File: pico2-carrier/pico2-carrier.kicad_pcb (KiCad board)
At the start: 2 copper layers, 81.8 x 80.8 mm, 52 parts, among them IC1 TFBS4711-TT1, IC2 M95512-DRMN8TP_K, IC3 IS25WP128F-JBLE, IC4 BQ25628ERYKR, J2 SCREEN_HDR, J3 DO0180FMST08, J5 Ext_Pwr_Rail, SW1 BUT_L, SW2 BUT_M, SW3 BUT_R, SW4 RUN, U1 Pico 2

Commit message: start work on PCB
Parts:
- removed BZ1: Speaker, Jumper:SolderJumper-2_P1.3mm_Open_Pad1.0x1.5mm
- removed the R4 at (173.5, 135.4)
- removed the R5 at (174.5, 134.4)
- added R3: 1k, Resistor_SMD:R_0402_1005Metric, F.Cu at (109.7, 130.3)
- BT1: footprint Jumper:SolderJumper-2_P1.3mm_Open_Pad1.0x1.5mm -> Connector_JST:JST_PH_B2B-PH-K_1x02_P2.00mm_Vertical
- IC1: value TFBS4711-TT1 -> TFDU4101-TT3; footprint SamacsysParts:TFBS4711TT1 -> SamacsysParts:TFDU4101-TR3
- IC2: value M95512-DRMN8TP_K -> M95512-DWDW4TP_K; footprint SamacsysParts:SOIC127P600X175-8N -> SamacsysParts:SOP65P640X120-8N
- IC3: value IS25WP128F-JBLE -> W25Q128JVSIM_TR
- R10: renamed from R6; value R -> 5k
- R8: renamed from R3; value 470R -> 1k
- R9: renamed from R7; value 470R -> 1k
- moved C13 66.3 mm to (173.0, 131.8), turned to -90 degrees
- moved C11 65.0 mm to (172.5, 123.7), turned to 180 degrees
- moved R8 19.8 mm to (166.9, 138.9), turned to 90 degrees
- moved D1 17.8 mm to (166.9, 136.9), turned to -90 degrees
- moved R9 17.7 mm to (164.8, 138.9), turned to 90 degrees
- moved D2 16.2 mm to (164.8, 136.9), turned to -90 degrees
- moved C3 11.8 mm to (161.3, 86.7), turned to 180 degrees
- moved IC3 9.85 mm to (164.6, 79.3)
- moved C6 9.29 mm to (168.4, 75.7)
- moved IC2 9.24 mm to (164.3, 84.4)
- moved H2 9.14 mm to (176.0, 72.6)
- moved JP3 8.79 mm to (166.6, 115.1)
- moved R1 8.47 mm to (141.2, 76.2), turned to -90 degrees
- moved C10 8.12 mm to (165.4, 131.1)
- moved C1 7.92 mm to (147.8, 75.7), turned to 180 degrees
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- renumbered C15 to C11, C11 to C12, C16 to C13, C12 to C14, C14 to C15, C13 to C16, H3 to H2, H2 to H3, J2 to J1, J3 to J2, J5 to J3, JP5 to JP3, JP3 to JP4, JP4 to JP5, R8 to R4, R9 to R5, SW4 to SW1, SW1 to SW2, SW2 to SW3, SW3 to SW4
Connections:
- net Net-(D1-K) renamed /battery-bq25628e/~{PG}
- net Net-(JP1-A) renamed /VBUS_OUT
- net Net-(JP2-A) renamed /VSYS_IN
- net Net-(JP5-A) renamed /3V3_OUT
- IC1 pad 2: /IR_PIO_TX -> unconnected-(IC1-IRED_CATHODE-Pad2)
- IC1 pad 3: /IR_PIO_RX -> /IR_PIO_TX
- IC1 pad 4: /IR_SD -> /IR_PIO_RX
- IC1 pad 5: /VCC1 -> /IR_SD
- IC1 pad 6: GND -> /VCC1
- IC4 pad 14: GND -> /~{BAT_CE}
- IC4 pad 22: GND -> /~{BAT_CE}
- IC4 pad 8: /battery-bq25628e/BAT -> /battery-bq25628e/BAT+
- SW1 pad 1: GND -> Net-(R3-Pad1)
- U1 pad 10: /ACCEL_INT1 -> /~{ACCEL_CSB}
- U1 pad 11: /~{FLASH_CSB} -> /ACCEL_INT1
- U1 pad 25: /~{BAT_INT} -> /BUT_L
- U1 pad 29: /BUT_L -> /BUT_M
- U1 pad 31: /BUT_M -> /BUT_R
- U1 pad 32: /BUT_R -> /~{BAT_CE}
- U1 pad 34: GND -> /~{BAT_INT}
- U1 pad 9: /~{ACCEL_CSB} -> /~{FLASH_CSB}
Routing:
- net +3.3V: track 0.00 -> 243.3 mm, vias 0 -> 10
- net /RUN: track 0.00 -> 58.0 mm
- net /I2C_SDA: track 6.82 -> 38.0 mm, vias 0 -> 2
- net /ACCEL_INT1: track 0.00 -> 30.1 mm
- net /I2C_SCL: track 6.18 -> 35.1 mm, vias 0 -> 2
- net /SPI_SCK: track 0.00 -> 28.6 mm, vias 0 -> 2
- net /~{BAT_CE}: track 0.00 -> 24.2 mm
- net /SPI_MOSI: track 0.00 -> 23.8 mm
- net /~{ACCEL_CSB}: track 0.00 -> 23.7 mm
- net /SPI_MISO: track 0.00 -> 23.6 mm
- net /IR_SD: track 0.00 -> 20.5 mm
- net VBUS: track 0.00 -> 20.1 mm, vias 0 -> 2
- net /IR_PIO_TX: track 0.00 -> 19.9 mm
- net /IR_PIO_RX: track 0.00 -> 19.2 mm
- net /BUT_L: track 0.00 -> 18.9 mm
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- added copper zone on B.Cu, net GND
- added copper zone on F.Cu, net GND
- added copper zone on In1.Cu, net GND
- added copper zone on In2.Cu, net GND
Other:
- board size 81.8 x 80.8 mm -> 81.8 x 71.6 mm
- copper layers 2 -> 4
- board text added: "3V3"
- board text added: "GND"

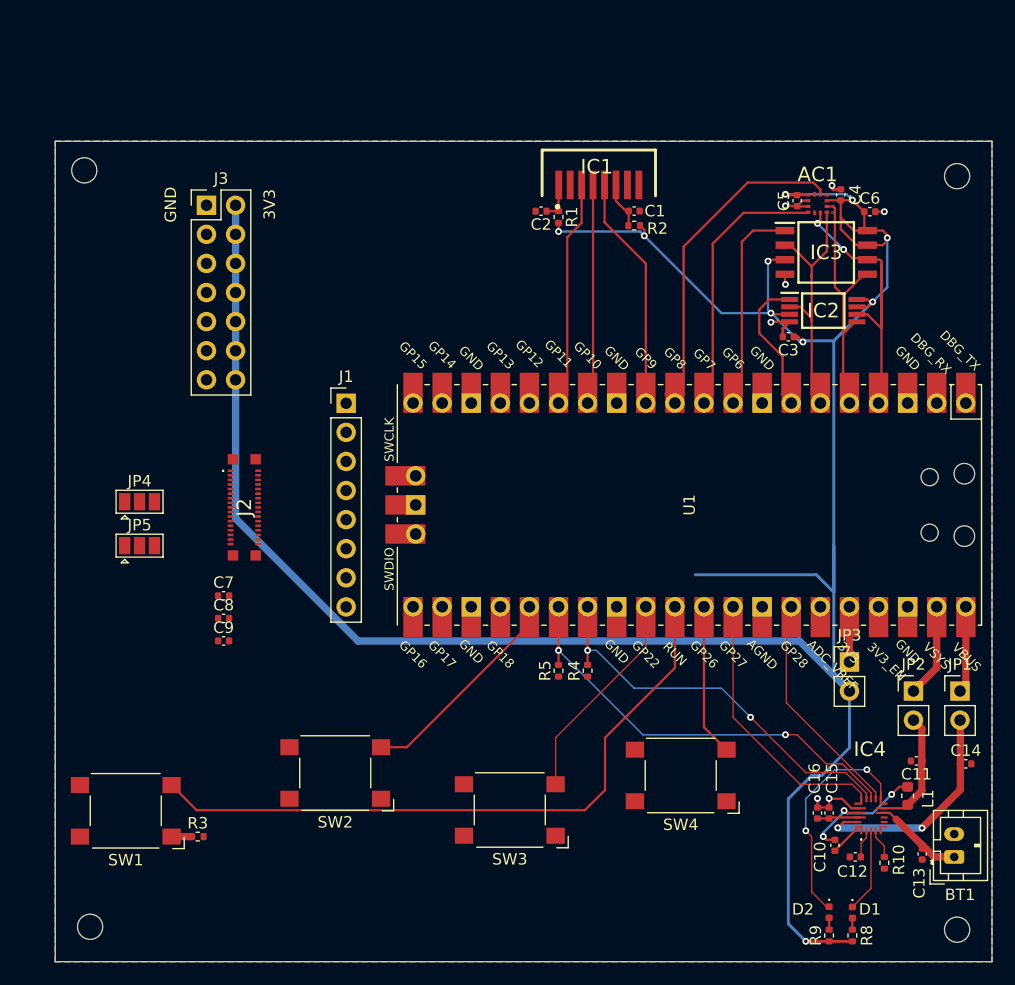
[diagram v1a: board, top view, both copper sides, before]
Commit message: finish routing - DRC ok
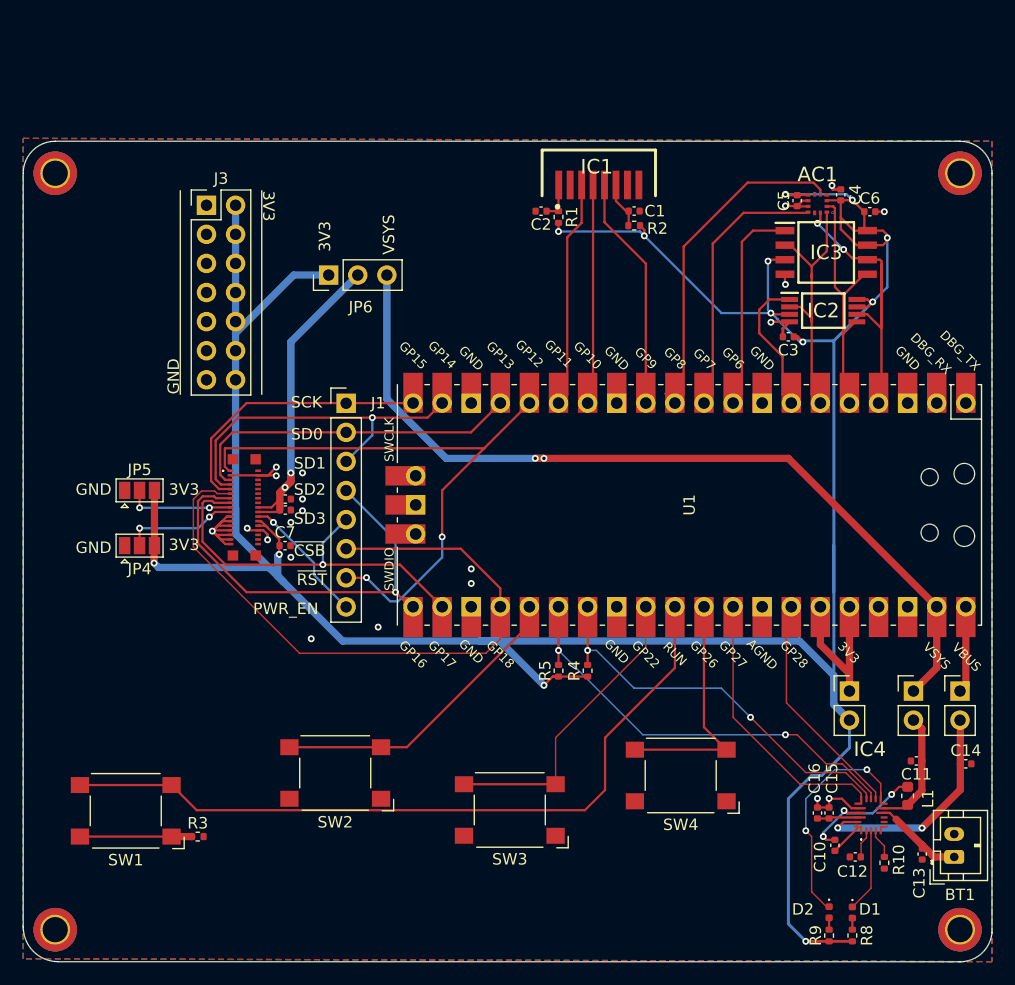
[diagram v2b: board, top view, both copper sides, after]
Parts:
- added JP6: SCREEN_PWR, Connector_PinHeader_2.54mm:PinHeader_1x03_P2.54mm_Vertical, F.Cu at (121.2, 81.3)
- H1, H2, H3, H4: footprint MountingHole:MountingHole_2.2mm_M2 -> MountingHole:MountingHole_2.2mm_M2_DIN965_Pad_TopBottom
- moved H2 102.6 mm to (97.3, 138.4)
- moved H4 101.2 mm to (176.3, 138.4)
- moved H3 66.0 mm to (176.3, 72.4)
- moved H1 65.9 mm to (97.3, 72.4)
- moved C9 12.6 mm to (117.4, 101.8)
- moved C8 11.7 mm to (117.4, 100.8)
- moved C7 6.92 mm to (117.3, 104.9)
- moved JP5 4.83 mm to (104.6, 100.1)
- moved JP4 3.84 mm to (104.6, 104.9)
- moved JP3 2.54 mm to (166.6, 117.6)
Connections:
- C8 pad 1: +3.3V -> /screen-headers/SCREEN_VBAT
- C9 pad 1: +3.3V -> /screen-headers/SCREEN_VBAT
- J2 pad 18: +3.3V -> /screen-headers/SCREEN_VBAT
- J2 pad 20: +3.3V -> /screen-headers/SCREEN_VBAT
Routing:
- net /VSYS_IN: track 8.20 -> 75.3 mm, vias 0 -> 2
- net /~{SCREEN_CSB}: track 0.00 -> 58.3 mm
- net /~{SCREEN_RST}: track 0.00 -> 52.3 mm, vias 0 -> 2
- net +3.3V: track 243.3 -> 282.4 mm, vias 10 -> 13
- net /HSTX_SD2: track 0.00 -> 38.5 mm, vias 0 -> 1
- net /HSTX_SD3: track 0.00 -> 34.0 mm, vias 0 -> 1
- net /HSTX_SD1: track 0.00 -> 30.8 mm, vias 0 -> 1
- net /HSTX_SD0: track 0.00 -> 29.7 mm
- net /screen-headers/SCREEN_VBAT: track 0.00 -> 29.6 mm, vias 0 -> 2
- net /HSTX_SCK: track 0.00 -> 24.6 mm
- net GND: track 15.4 -> 37.0 mm, vias 7 -> 21
- net /screen-headers/PWR_EN: track 0.00 -> 11.6 mm, vias 0 -> 1
- net /screen-headers/IM0: track 0.00 -> 10.3 mm, vias 0 -> 2
- net /screen-headers/IM1: track 0.00 -> 9.48 mm, vias 0 -> 2
- net /3V3_OUT: track 4.82 -> 14.3 mm
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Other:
- board size 81.8 x 71.6 mm -> 84.6 x 71.6 mm
- board text added: "PWR_EN"
- board text added: "SCK"
- board text added: "SD0"
- board text added: "SD1"
- board text added: "SD2"
- board text added: "SD3"
- board text added: "VSYS"
- board text added: "~{CSB}"
- board text added: "~{RST}"

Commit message: pcb tweaks
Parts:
- moved R3 7.47 mm to (102.6, 128.0), turned to -90 degrees
- moved SW1 6.55 mm to (104.9, 121.7), turned to 90 degrees
- moved JP6 1.52 mm to (121.2, 82.8)
- moved C2 0.50 mm to (139.7, 76.2)
- moved R1 0.50 mm to (141.2, 76.7)
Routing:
- net +3.3V: track 282.4 -> 275.2 mm
- net /screen-headers/SCREEN_VBAT: track 29.6 -> 27.6 mm
- net VBUS: track 20.1 -> 21.8 mm, vias 2 -> 4
- net /VSYS_IN: track 75.3 -> 73.8 mm
- net /battery-bq25628e/STAT: track 20.4 -> 19.7 mm
- net GND: track 37.0 -> 37.2 mm, vias 21 -> 169
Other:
- board text added: "+"
- board text added: "-"
- board text added: "Accel"
- board text added: "EEPROM"
- board text added: "Ext. Power"
- board text added: "Flash"
- board text added: "IM0"
- board text added: "IM1"
- board text added: "IrDA"
- board text added: "Left"
- board text added: "Middle"
- board text added: "PMIC"
- board text added: "RUN"
- board text added: "Right"
- board text added: "Screen"
- board text added: "Screen Header"
- board text added: "Screen Power"

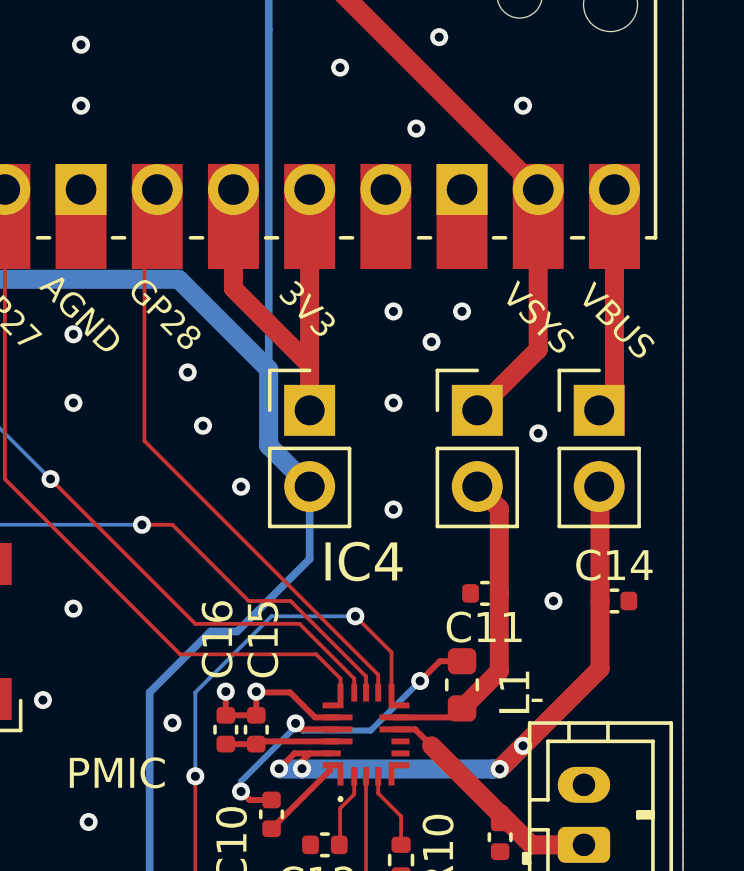
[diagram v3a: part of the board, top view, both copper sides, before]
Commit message: add PFET to VSYS input
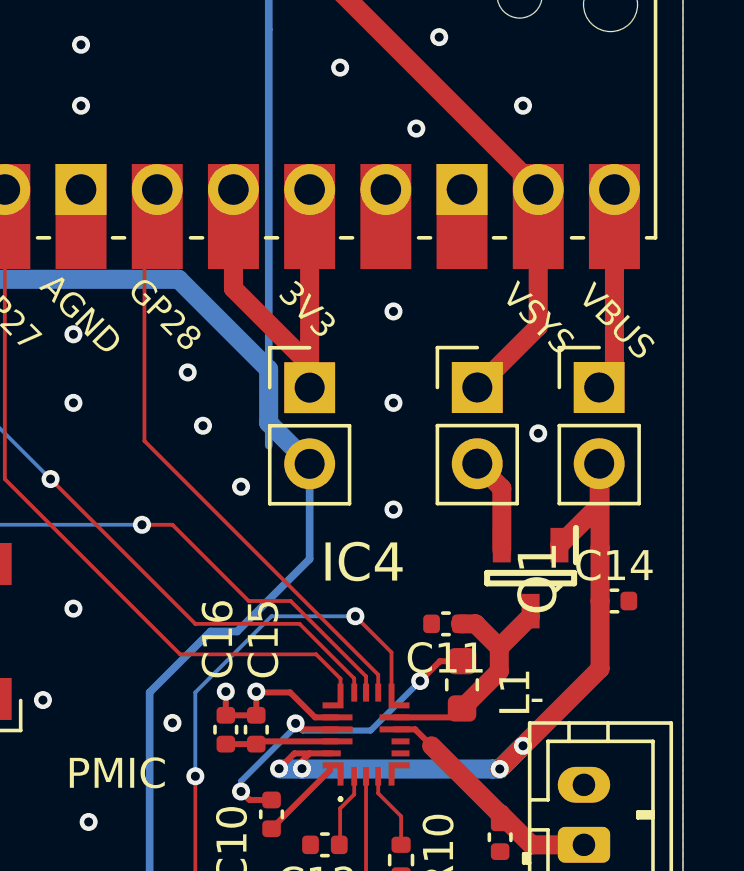
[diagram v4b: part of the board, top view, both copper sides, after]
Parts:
- added Q1: DMG2305UX-7, SamacsysParts:SOT96P240X115-3N, F.Cu at (174.0, 123.2)
- moved C11 1.65 mm to (171.2, 124.7)
- moved JP1 0.76 mm to (176.3, 116.8)
- moved JP2 0.76 mm to (172.2, 116.8)
- moved JP3 0.76 mm to (166.6, 116.8)
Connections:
- C11 pad 1: VSYS -> /battery-bq25628e/SYS
- IC4 pad 9: VSYS -> /battery-bq25628e/SYS
- L1 pad 2: VSYS -> /battery-bq25628e/SYS
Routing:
- net /battery-bq25628e/SYS: track 0.00 -> 8.02 mm
- net VSYS: track 10.6 -> 3.22 mm
- net VBUS: track 21.8 -> 26.0 mm
- net +3.3V: track 275.2 -> 273.3 mm
- net /VSYS_IN: track 73.8 -> 73.0 mm
- net /VBUS_OUT: track 8.29 -> 7.53 mm
- net GND: vias 169 -> 166
